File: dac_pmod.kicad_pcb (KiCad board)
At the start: 2 copper layers, 38.7 x 18.4 mm, 14 parts, among them J1 Conn_02x06_Top_Bottom, J2 Conn_02x04_Odd_Even, U1 MCP6004

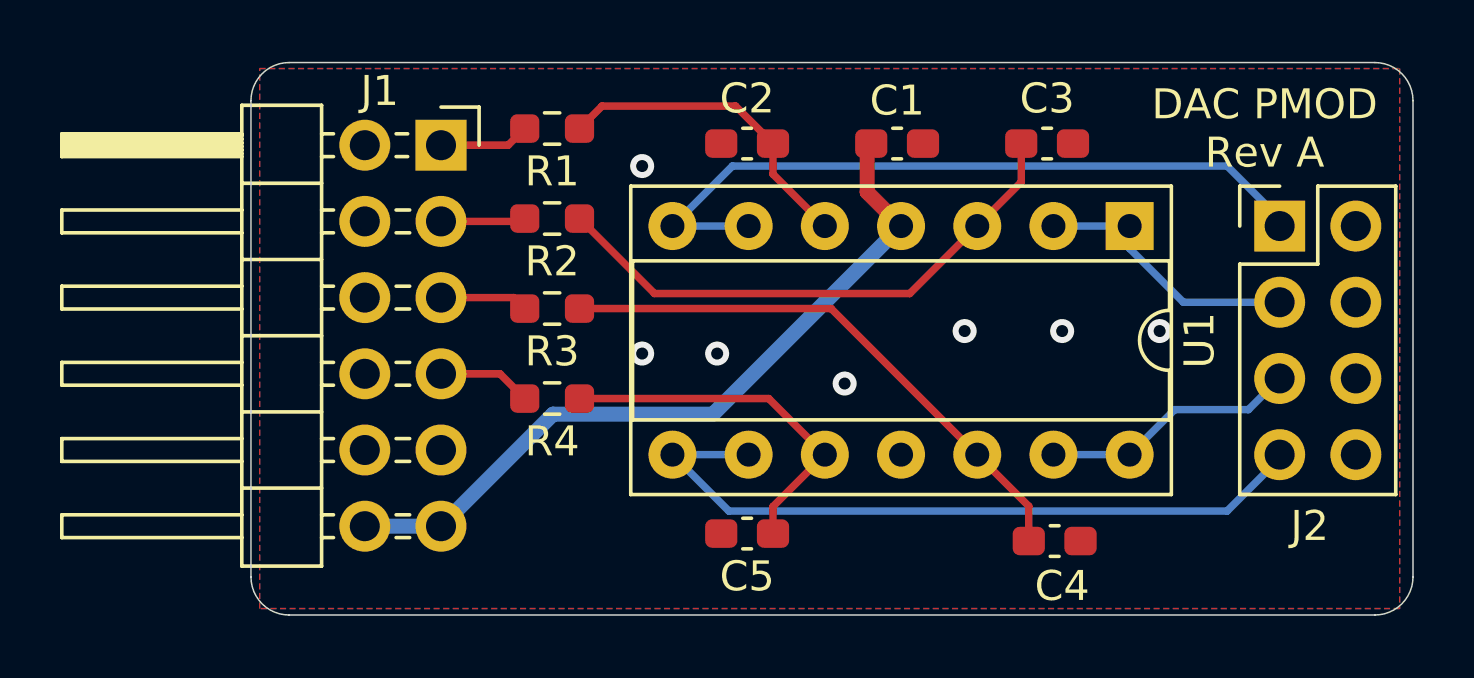
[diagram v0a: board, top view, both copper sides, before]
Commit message: Update to 4-layer design because... why not.
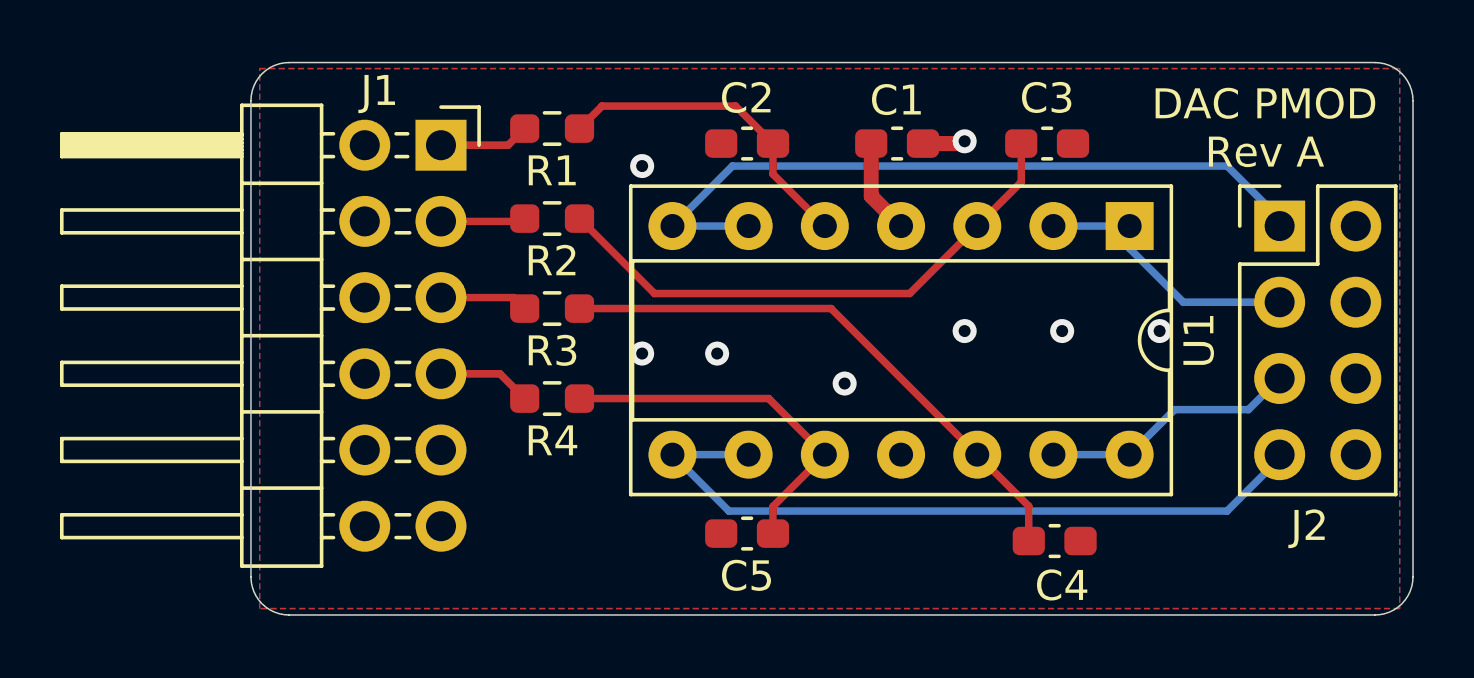
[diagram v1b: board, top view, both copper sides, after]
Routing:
- net +3V3: track 25.3 -> 3.16 mm
- net GND: track 0.00 -> 1.46 mm, vias 7 -> 8
- added copper zone on In2.Cu, net +3V3
- added copper zone on In1.Cu, net GND
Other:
- copper layers 2 -> 4
